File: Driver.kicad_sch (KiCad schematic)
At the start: 26 parts, among them Q1 SQJ886EP-T1_GE3, Q3 SQJ886EP-T1_GE3, Q5 SQJ886EP-T1_GE3, Q7 SQJ886EP-T1_GE3, U1 UCC21520DW, U4 UCC21520DW

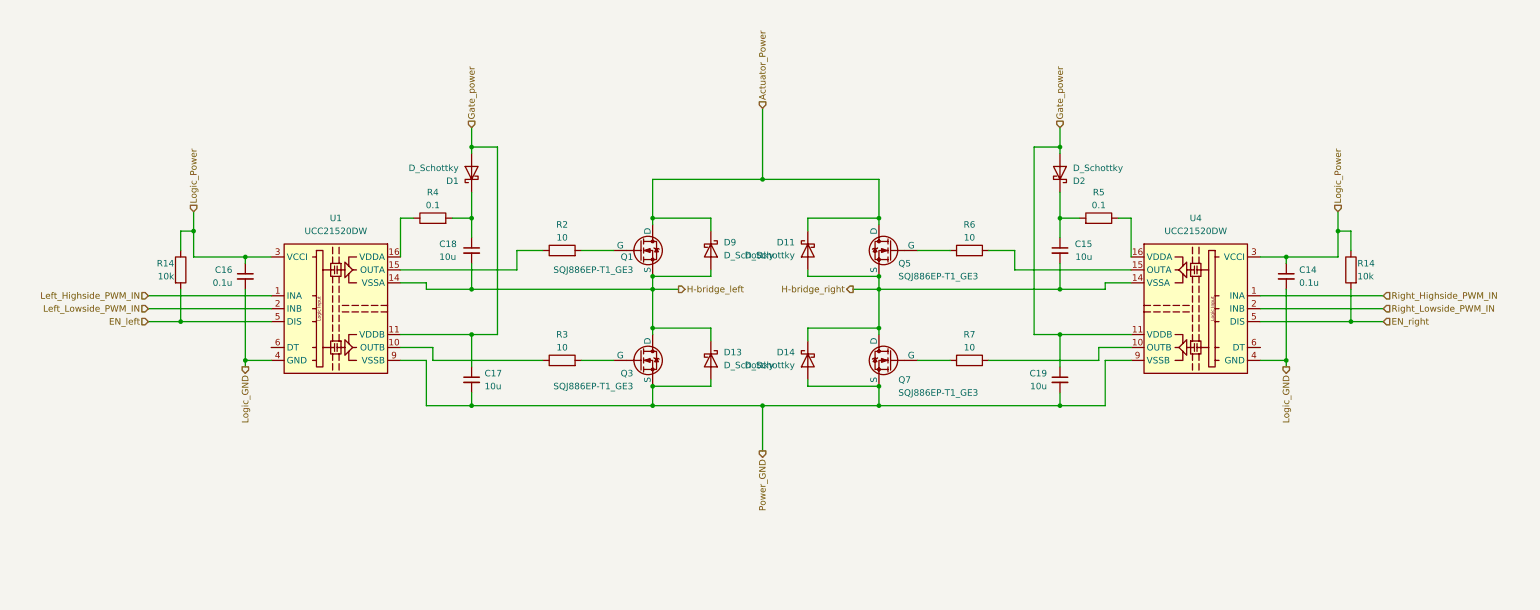
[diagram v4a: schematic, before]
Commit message: add MOSFET pulldown
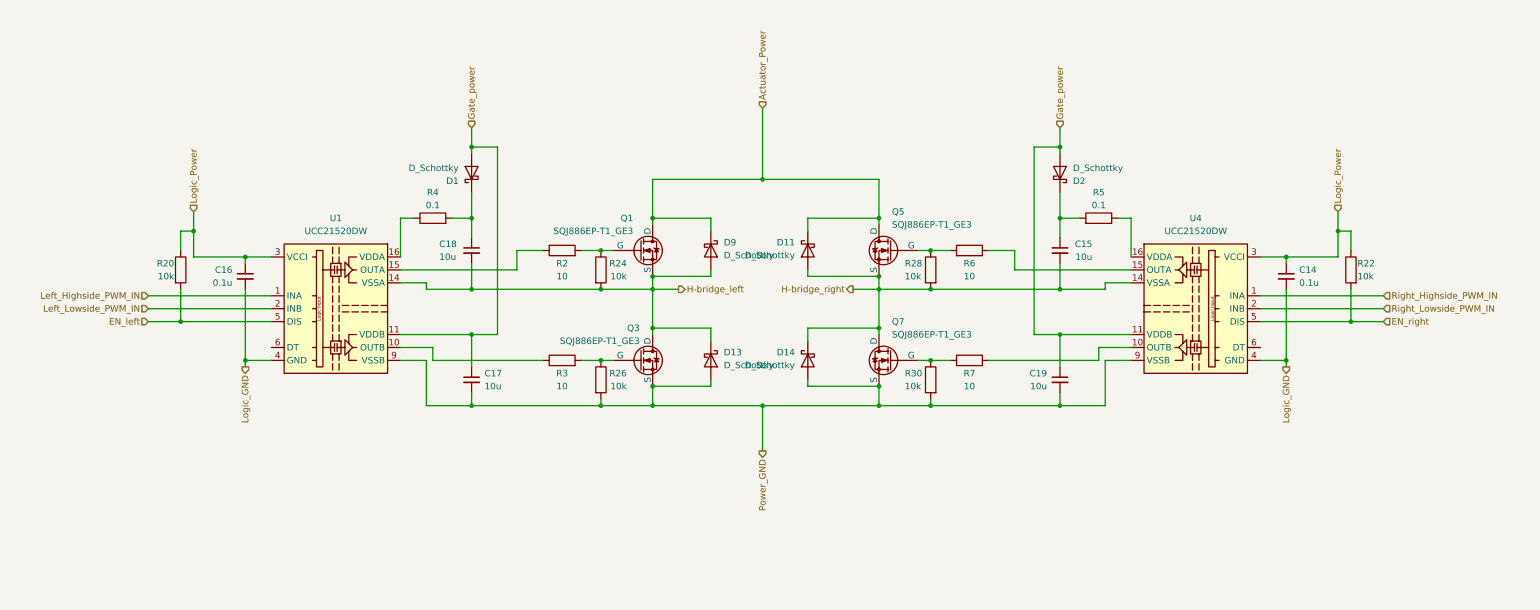
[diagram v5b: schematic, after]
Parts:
- added R24, R26, R28, R30: 10k, Resistor_SMD:R_0402_1005Metric_Pad0.72x0.64mm_HandSolder, symbol Device:R
- renumbered R14 to R20, R14 to R22
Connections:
- net H-bridge_left: now also R24.2
- net H-bridge_right: now also R28.2
- net Power_GND: now also R26.2, R30.2
- net at Q1.4 (G), R2.2: now also R24.1
- net at Q7.4 (G), R7.2: now also R30.1
- net at Q3.4 (G), R3.2: now also R26.1
- net at Q5.4 (G), R6.2: now also R28.1

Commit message: fix drive circuit
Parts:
- R24, R26, R28, R30: value 10k -> 20k
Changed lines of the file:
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@@
       (effects (font (size 1.27 1.27)) (justify right))
     )
-    (property "Value" "10k" (at 121.92 125.73 0)
+    (property "Value" "20k" (at 121.92 125.73 0)
       (effects (font (size 1.27 1.27)) (justify right))
     )
@@
       (effects (font (size 1.27 1.27)) (justify right))
     )
-    (property "Value" "10k" (at 121.92 104.14 0)
+    (property "Value" "20k" (at 121.92 104.14 0)
       (effects (font (size 1.27 1.27)) (justify right))
     )
@@
       (effects (font (size 1.27 1.27)) (justify right))
     )
-    (property "Value" "10k" (at 176.53 104.14 0)
+    (property "Value" "20k" (at 176.53 104.14 0)
       (effects (font (size 1.27 1.27)) (justify right))
     )
@@
       (effects (font (size 1.27 1.27)) (justify right))
     )
-    (property "Value" "10k" (at 176.53 125.73 0)
-      (effects (font (size 1.27 1.27)) (justify right))
-    )
+    (property "Value" "20k" (at 176.53 125.73 0)
+      (effects (font (size 1.27 1.27)) (justify right))
+    )

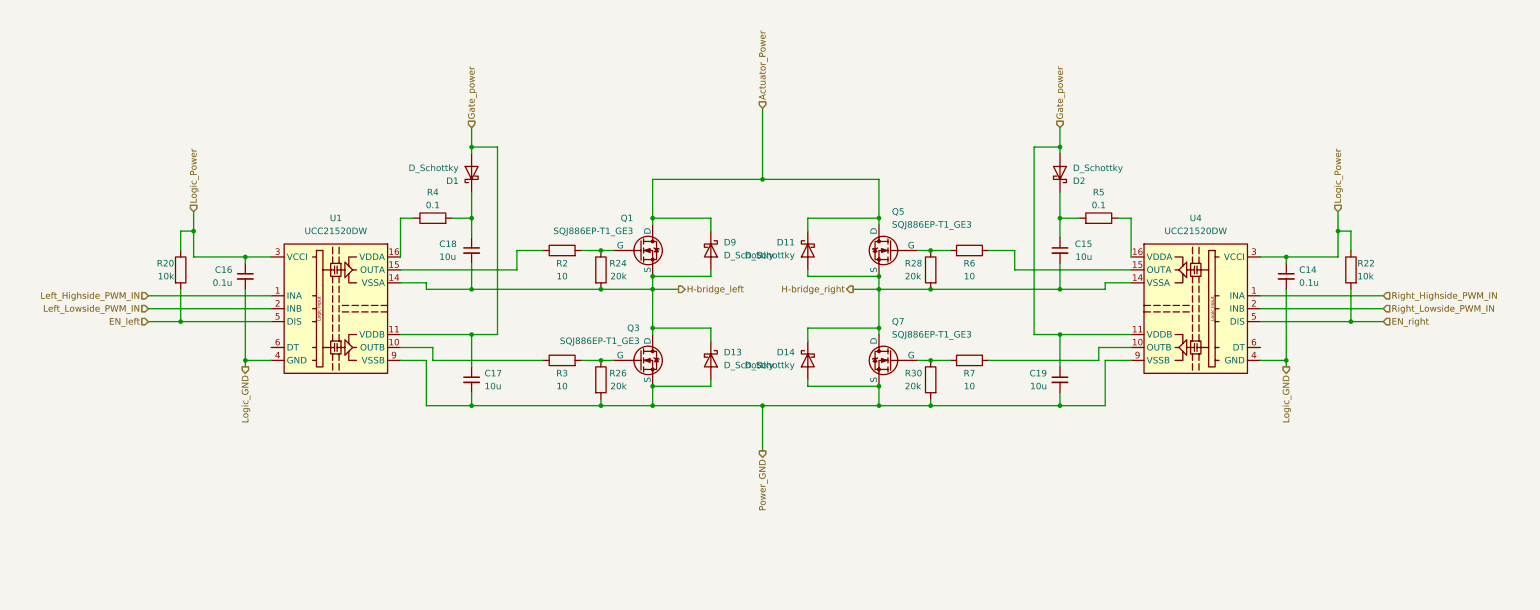
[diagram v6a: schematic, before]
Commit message: add logic parts
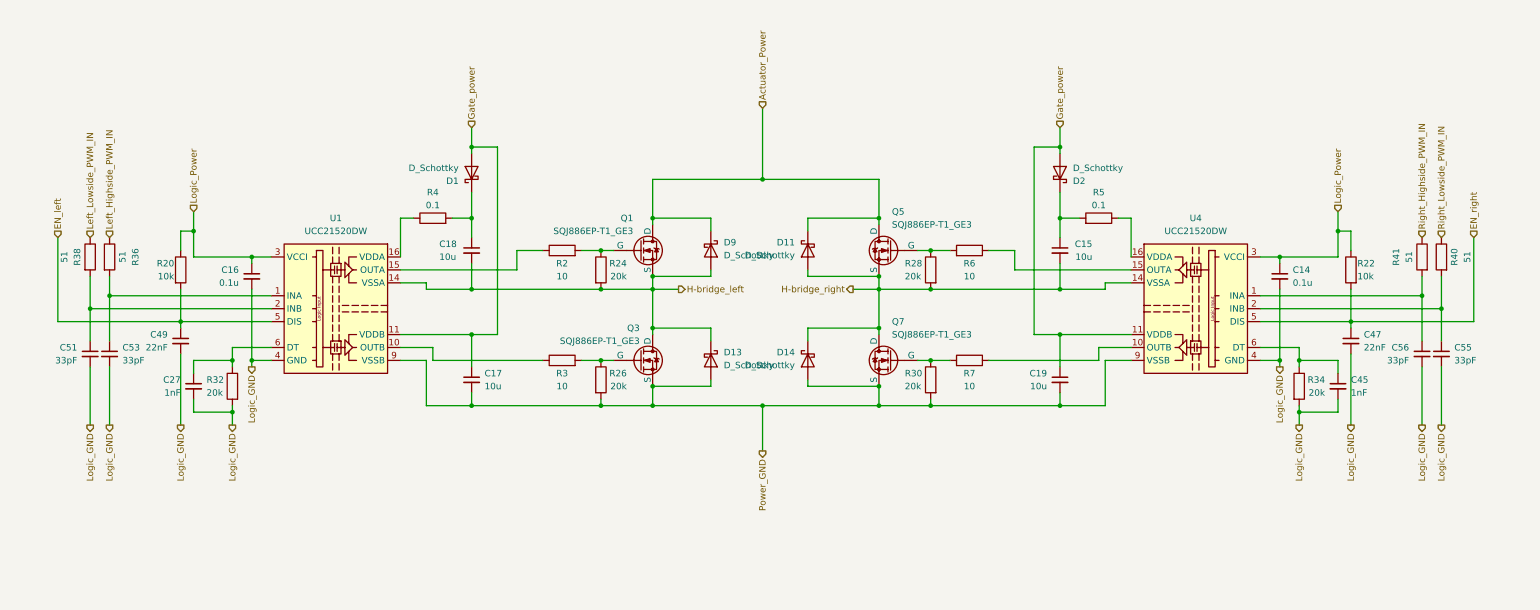
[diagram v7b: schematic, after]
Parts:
- added C27, C45: 1nF, Capacitor_SMD:C_0402_1005Metric_Pad0.74x0.62mm_HandSolder, symbol Device:C_Small
- added C47, C49: 22nF, Capacitor_SMD:C_0402_1005Metric_Pad0.74x0.62mm_HandSolder, symbol Device:C_Small
- added C51, C53, C55, C56: 33pF, Capacitor_SMD:C_0603_1608Metric_Pad1.08x0.95mm_HandSolder, symbol Device:C_Small
- added R32, R34: 20k, Resistor_SMD:R_0402_1005Metric_Pad0.72x0.64mm_HandSolder, symbol Device:R
- added R36, R38, R40, R41: 51, Resistor_SMD:R_0603_1608Metric_Pad0.98x0.95mm_HandSolder, symbol Device:R
- C14, C16: footprint Capacitor_SMD:C_01005_0402Metric_Pad0.57x0.30mm_HandSolder -> Capacitor_SMD:C_0402_1005Metric_Pad0.74x0.62mm_HandSolder
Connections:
- net EN_left: now also C49.1
- net EN_right: now also C47.1
- net Left_Highside_PWM_IN: now also R36.1; no longer U1.1 (INA)
- net Left_Lowside_PWM_IN: now also R38.1; no longer U1.2 (INB)
- net Logic_GND: now also C27.2, C45.2, C47.2, C49.2, C51.2, C53.2, C55.2, C56.2, R32.2, R34.2
- net Right_Highside_PWM_IN: now also R41.1; no longer U4.1 (INA)
- net Right_Lowside_PWM_IN: now also R40.1; no longer U4.2 (INB)
- net at U4.6 (DT): now also C45.1, R34.1
- net at U1.6 (DT): now also C27.1, R32.1
- new net: C56.1, R41.2, U4.1 (INA)
- new net: C55.1, R40.2, U4.2 (INB)
- new net: C53.1, R36.2, U1.1 (INA)
- new net: C51.1, R38.2, U1.2 (INB)
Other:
- moved on the sheet: C14, C16
